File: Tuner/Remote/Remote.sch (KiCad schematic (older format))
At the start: 101 parts, among them J1 Conn_01x05, J10 Conn_01x05, J11 Conn_01x04, J12 Conn_01x04, J13 Conn_01x01, J14 Conn_01x01, J15 Conn_01x02, J16 Conn_01x06, J17 Conn_01x02, J18 Conn_01x01, J19 Conn_01x01, J2 Conn_01x05, J20 Conn_01x01, J21 Conn_01x01, J22 Conn_01x01, J23 Conn_01x01, J24 Conn_01x02, J26 Conn_01x02, J27 Conn_01x02, J3 USB_B, J4 Conn_01x04, J5 Conn_01x20, J6 Conn_02x03_Odd_Even, J7 Conn_01x02, J8 Conn_01x06, J9 Conn_01x20, Q1 2N7000, Q2 2N7000, Q3 2N7000, Q4 2N7000, U1 LM1117-3.3, U2 STM32F103C8T6, U3 LM7805_TO220, U4 LM7805_TO220, Y1 8 MHz, Y2 Crystal

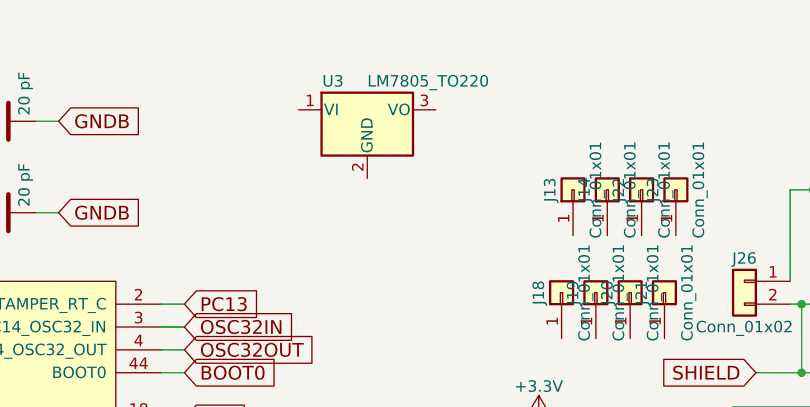
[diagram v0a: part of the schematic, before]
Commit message: added Bill of Materials
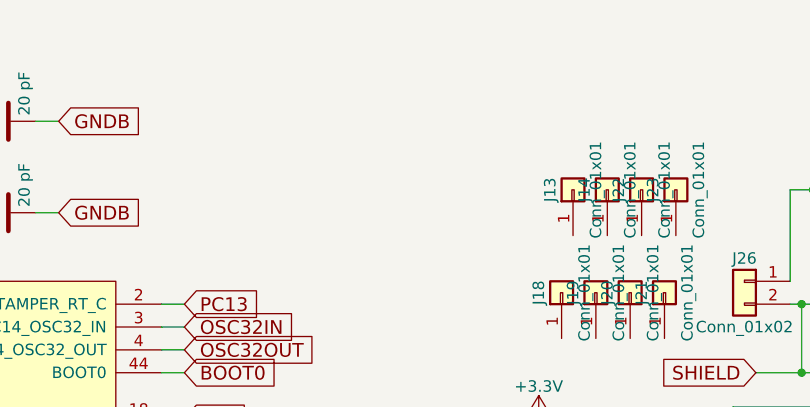
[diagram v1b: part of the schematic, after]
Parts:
- removed U3: LM7805_TO220, TO_SOT_Packages_THT:TO-220_Vertical, symbol LM7805_TO220
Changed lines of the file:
@@
-$EndComp
-$Comp
-L LM7805_TO220 U3
-U 1 1 5B661CB4
-P 5400 650
-F 0 "U3" H 5250 775 50  0000 C CNN
-F 1 "LM7805_TO220" H 5400 775 50  0000 L CNN
-F 2 "TO_SOT_Packages_THT:TO-220_Vertical" H 5400 875 50  0001 C CIN
-F 3 "" H 5400 600 50  0001 C CNN
-	1    5400 650
-	1    0    0    -1
 $EndComp
 $Comp

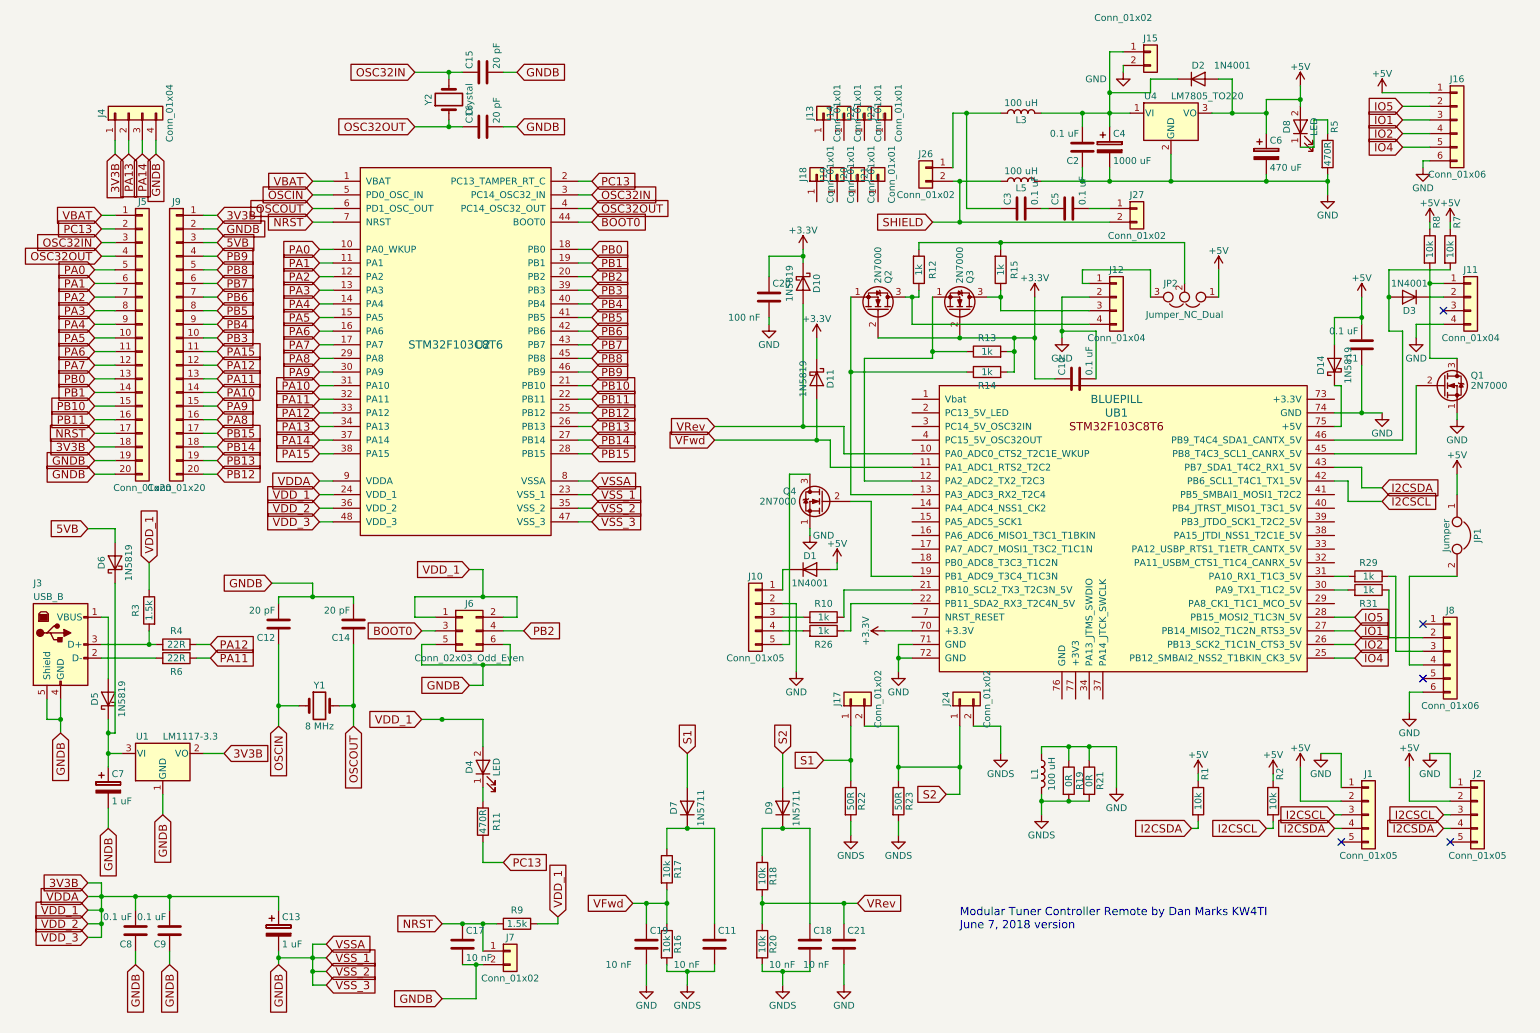
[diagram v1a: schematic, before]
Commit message: JLCPCB order 09232018 - improved grounding - improved I2C cabling - NEO7M port - support for common mode chokes - relay board now has capacitors on all coils
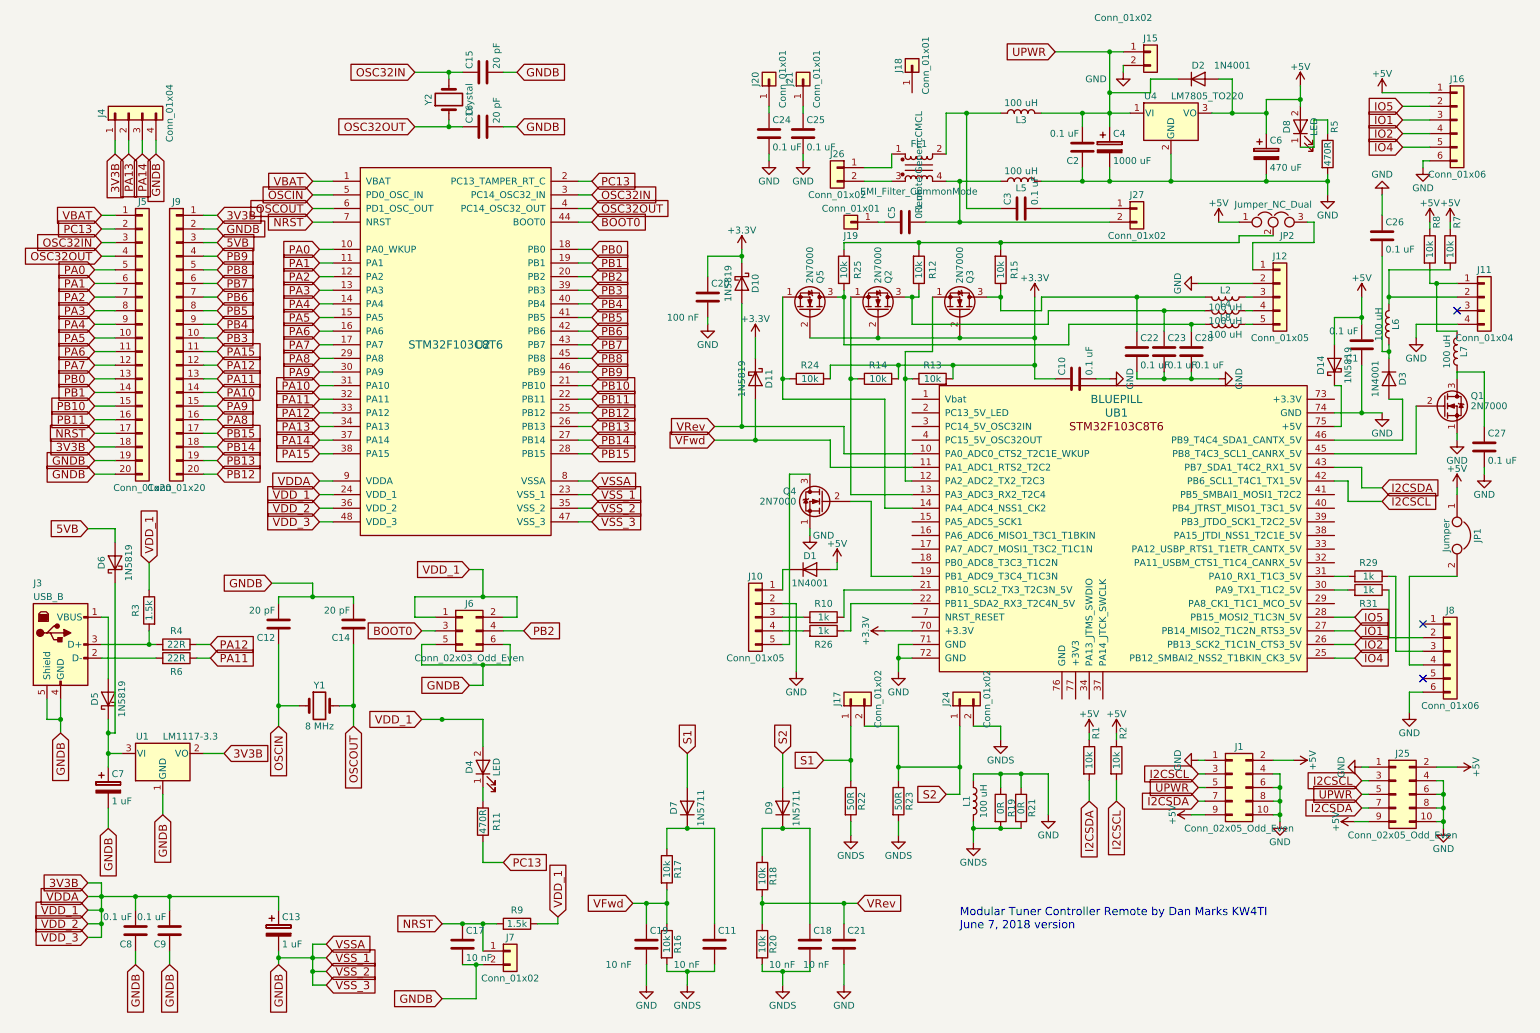
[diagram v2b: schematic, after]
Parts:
- removed J1, J2: Conn_01x05, Connectors_Molex:Molex_KK-6410-05_05x2.54mm_Straight, symbol Conn_01x05
- removed J12: Conn_01x04, Connectors_Molex:Molex_KK-6410-04_04x2.54mm_Straight, symbol Conn_01x04
- removed J13, J14, J22, J23: Conn_01x01, Connectors:1pin, symbol Conn_01x01
- added C22, C23, C24, C25, C26, C27, C28: 0.1 uF, Capacitors_THT:C_Disc_D5.0mm_W2.5mm_P2.50mm, symbol C
- added FL1: EMI_Filter_CommonMode, Remote:GenericCMCL, symbol EMI_Filter_CommonMode
- added J1, J25: Conn_02x05_Odd_Even, Pin_Headers:Pin_Header_Straight_2x05_Pitch2.54mm, symbol Conn_02x05_Odd_Even
- added J12: Conn_01x05, Pin_Headers:Pin_Header_Straight_1x05_Pitch2.54mm, symbol Conn_01x05
- added L2, L4, L6, L7, L8: 100 uH, Inductors_THT:L_Axial_L5.3mm_D2.2mm_P7.62mm_Horizontal_Vishay_IM-1, symbol L
- added Q5: 2N7000, TO_SOT_Packages_THT:TO-92_Molded_Narrow, symbol 2N7000
- added R24, R25: 10k, Resistors_THT:R_Axial_DIN0207_L6.3mm_D2.5mm_P7.62mm_Horizontal, symbol R
- C1, C10, C11, C18, C19, C2, C20, C21: footprint Capacitors_THT:C_Disc_D5.1mm_W3.2mm_P5.00mm -> Capacitors_THT:C_Disc_D5.0mm_W2.5mm_P2.50mm
- J11: footprint Connectors_Molex:Molex_KK-6410-04_04x2.54mm_Straight -> Pin_Headers:Pin_Header_Straight_1x04_Pitch2.54mm
- R12, R13, R14, R15: value 1k -> 10k
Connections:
- net +3V3: now also Q5.2 (G), R24.2
- net +5V: now also J1.2 (Pin_2), J1.9 (Pin_9), J25.2 (Pin_2), J25.9 (Pin_9)
- net GND: now also C22.2, C23.2, C24.2, C25.2, C26.1, C27.2, C28.2, J1.1 (Pin_1), J1.10 (Pin_10), J1.4 (Pin_4), J1.6 (Pin_6), J1.8 (Pin_8), J12.2 (Pin_2), J25.1 (Pin_1), J25.10 (Pin_10), J25.4 (Pin_4), J25.6 (Pin_6), J25.8 (Pin_8)
- net I2CSCL: now also J1.3 (Pin_3), J25.3 (Pin_3)
- net I2CSDA: now also J1.7 (Pin_7), J25.7 (Pin_7)
- net at J19.1 (Pin_1): now also C5.1
- net at J20.1 (Pin_1): now also C24.1
- net at J21.1 (Pin_1): now also C25.1
- net at C3.2: now also J27.1 (Pin_1); no longer C5.1
- net at C5.2: now also J27.2 (Pin_2), L5.1, FL1.4; no longer J27.1 (Pin_1)
- net at UB1.14 (PA4_ADC4_NSS1_CK2): now also Q5.1 (S), R24.1
- net at D3.2 (A), UB1.46 (PB9_T4C4_SDA1_CANTX_5V): no longer R7.2
- net UPWR: now reaches C2.2, C4.1, D2.1 (K), J15.1 (Pin_1), L3.2, U4.1 (VI)
- net UPWR: now also J1.5 (Pin_5), J25.5 (Pin_5)
- net at C3.1, L3.1: now also FL1.2; no longer J26.1 (Pin_1)
- net at JP2.3: now also J12.1 (Pin_1)
- net at Q3.3 (D), R15.1: now also C22.1, L2.2
- net at Q2.3 (D), R12.1: now also C23.1, L4.2
- net at JP2.2, R12.2, R15.2: now also R25.1
- net at J11.1 (Pin_1), R8.2: now also L7.2; no longer Q1.3 (D)
- net at J11.2 (Pin_2): now also R7.2, L6.2; no longer D3.1 (K)
- removed net SHIELD: J26.2 (Pin_2), J27.2 (Pin_2), L5.1
- new net: FL1.1, J26.1 (Pin_1)
- new net: FL1.3, J26.2 (Pin_2)
- new net: C26.2, D3.1 (K), L6.1
- new net: C27.1, L7.1, Q1.3 (D)
- new net: J12.3 (Pin_3), L2.1
- new net: J12.4 (Pin_4), L4.1
- new net: C28.1, L8.2, Q5.3 (D), R25.2
- new net: J12.5 (Pin_5), L8.1
- no-connect marks 5 -> 3
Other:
- moved on the sheet: C20, D10, D11, D3, J11, J18, J19, J20, J21, J26, JP2, L1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

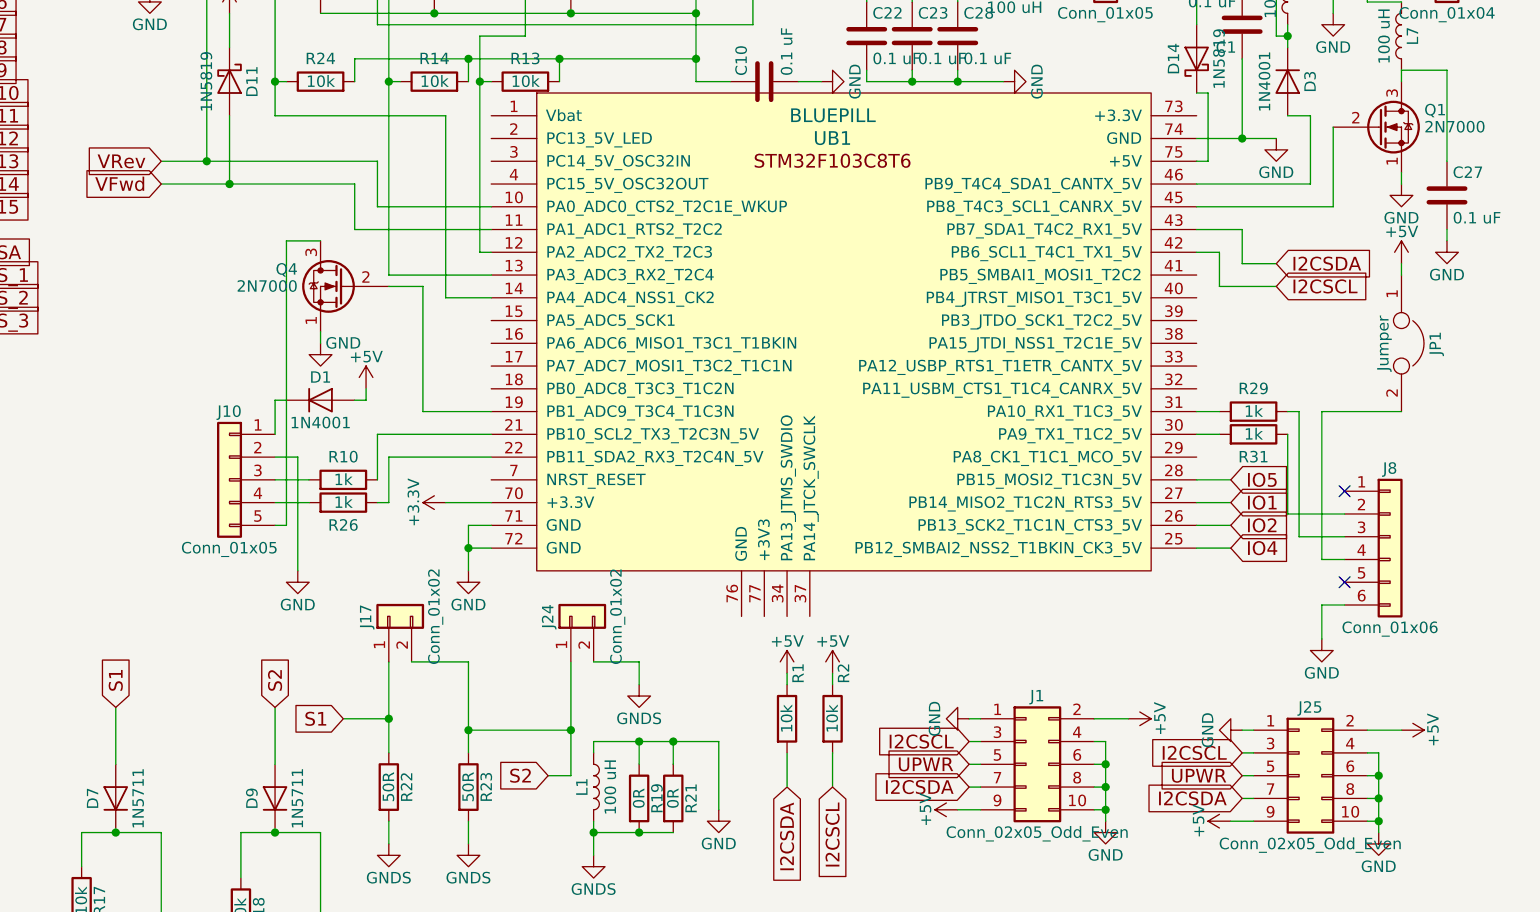
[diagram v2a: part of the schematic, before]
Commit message: Changed I2C cable pinoutgit add Tunergit add Tuner Also added ICOM rig support
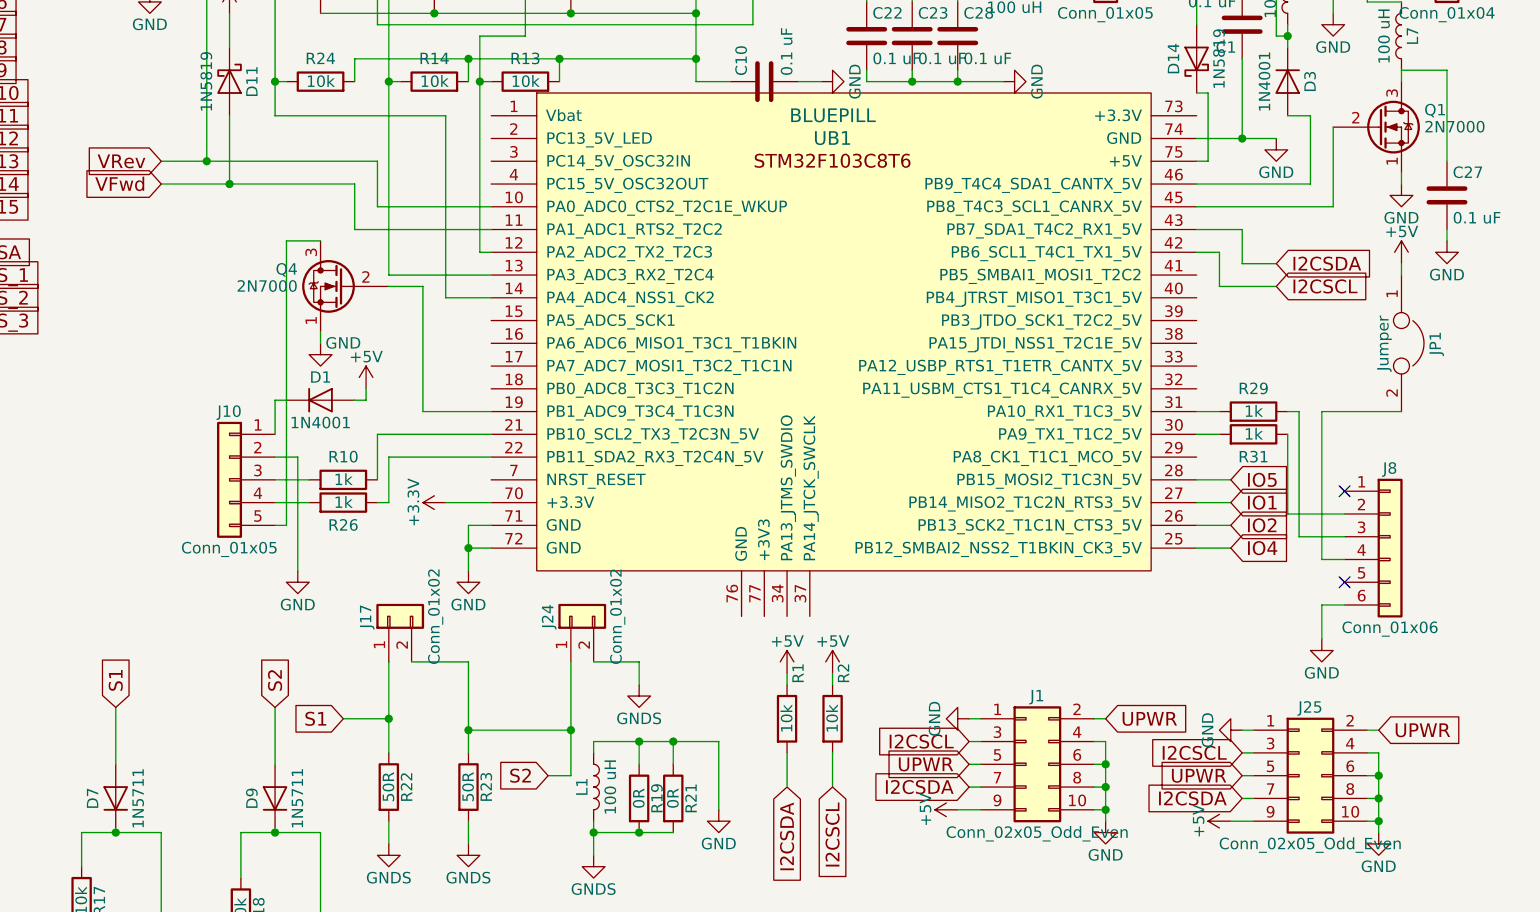
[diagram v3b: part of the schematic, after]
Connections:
- net +5V: no longer J1.2 (Pin_2), J25.2 (Pin_2)
- net UPWR: now also J1.2 (Pin_2), J25.2 (Pin_2)
